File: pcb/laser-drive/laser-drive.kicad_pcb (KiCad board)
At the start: 2 copper layers, 28.6 x 32.4 mm, 28 parts, among them J1 CONN_01X03, P1 LaserOut, Q1 BCP5616Q, Q2 MTM232270, U2 MIC920

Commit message: o Change footprint trimmer to actual size.
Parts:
- RV1: footprint Potentiometers:Potentiometer_WirePads -> Potentiometers:Potentiometer_WirePads_Small
- moved RV1 5.26 mm to (95.9, 48.3)
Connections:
- net LASER_DATA renamed Net-(J1-Pad2)
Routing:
- net GND: track 127.1 -> 130.9 mm
- net /VRef: track 10.4 -> 12.8 mm

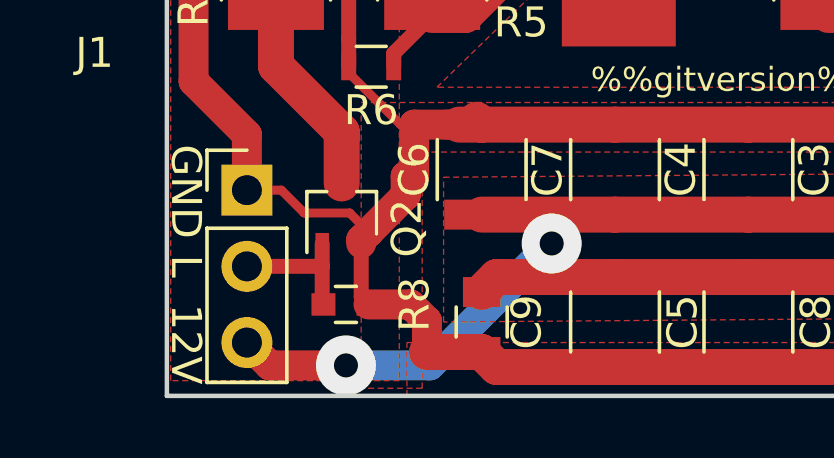
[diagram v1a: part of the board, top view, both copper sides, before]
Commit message: o Update footprint resistor.
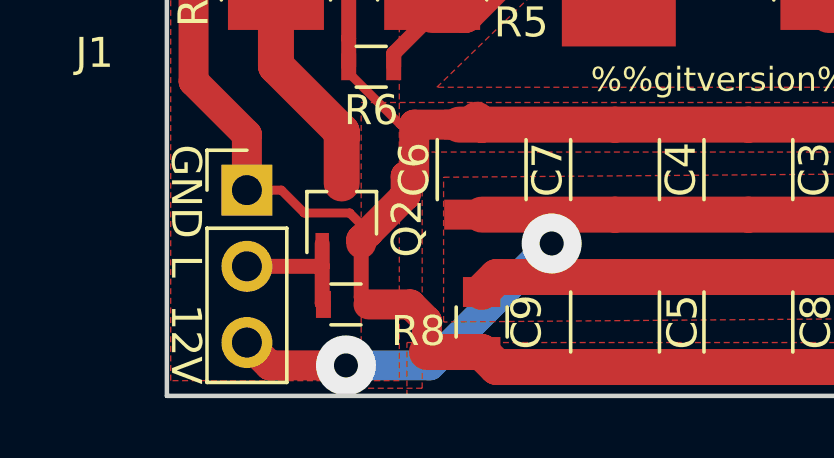
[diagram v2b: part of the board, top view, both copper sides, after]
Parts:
- R8: value 100k -> 1k; footprint Capacitors_SMD:C_0603 -> Resistors_SMD:R_0603
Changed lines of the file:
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@@
-(kicad_pcb (version 20170123) (host pcbnew "(2017-03-23 revision f2763e90e)-master")
+(kicad_pcb (version 20170123) (host pcbnew "(2017-04-01 revision 6eb2000b6)-master")
   (general
     (links 48)
@@
     )
   )
-  (module Capacitors_SMD:C_0603 (layer F.Cu)
-    (at 89.154 74.422 180)
-    (descr "Capacitor SMD 0603, reflow soldering, AVX (see smccp.pdf)")
-    (tags "capacitor 0603")
-    (attr smd)
-    (fp_text reference R8 (at -2.286 0 90) (layer F.SilkS)
-      (effects (font (size 1 1) (thickness 0.15)))
-    )
-    (fp_text value 100k (at 0 1.5 180) (layer F.Fab)
-      (effects (font (size 1 1) (thickness 0.15)))
-    )
-    (fp_line (start 1.4 0.65) (end -1.4 0.65) (layer F.CrtYd) (width 0.05))
-    (fp_line (start 1.4 0.65) (end 1.4 -0.65) (layer F.CrtYd) (width 0.05))
-    (fp_line (start -1.4 -0.65) (end -1.4 0.65) (layer F.CrtYd) (width 0.05))
-    (fp_line (start -1.4 -0.65) (end 1.4 -0.65) (layer F.CrtYd) (width 0.05))
-    (fp_line (start 0.35 0.6) (end -0.35 0.6) (layer F.SilkS) (width 0.12))
-    (fp_line (start -0.35 -0.6) (end 0.35 -0.6) (layer F.SilkS) (width 0.12))
-    (fp_line (start -0.8 -0.4) (end 0.8 -0.4) (layer F.Fab) (width 0.1))
-    (fp_line (start 0.8 -0.4) (end 0.8 0.4) (layer F.Fab) (width 0.1))
-    (fp_line (start 0.8 0.4) (end -0.8 0.4) (layer F.Fab) (width 0.1))
-    (fp_line (start -0.8 0.4) (end -0.8 -0.4) (layer F.Fab) (width 0.1))
-    (fp_text user %R (at 0 -1.5 180) (layer F.Fab)
-      (effects (font (size 1 1) (thickness 0.15)))
-    )
-    (pad 2 smd rect (at 0.75 0 180) (size 0.8 0.75) (layers F.Cu F.Paste F.Mask)
-      (net 12 "Net-(J1-Pad2)"))
-    (pad 1 smd rect (at -0.75 0 180) (size 0.8 0.75) (layers F.Cu F.Paste F.Mask)
-      (net 1 GND))
-    (model Capacitors_SMD.3dshapes/C_0603.wrl
-      (at (xyz 0 0 0))
-      (scale (xyz 1 1 1))
-      (rotate (xyz 0 0 0))
-    )
-  )
   (module TO_SOT_Packages_SMD:SOT-323_SC-70 (layer F.Cu)
     (at 89.012 71.39 90)
@@
       (scale (xyz 1 1 1))
       (rotate (xyz 0 0 0))
+    )
+  )
+  (module Resistors_SMD:R_0603 (layer F.Cu)
+    (at 89.154 74.422 180)
+    (descr "Resistor SMD 0603, reflow soldering, Vishay (see dcrcw.pdf)")
+    (tags "resistor 0603")
+    (attr smd)
+    (fp_text reference R8 (at -2.413 -0.889 180) (layer F.SilkS)
+      (effects (font (size 1 1) (thickness 0.15)))
+    )
+    (fp_text value 1k (at 0 1.5 180) (layer F.Fab)
+      (effects (font (size 1 1) (thickness 0.15)))
+    )
+    (fp_text user %R (at 0 -1.45 180) (layer F.Fab)
+      (effects (font (size 1 1) (thickness 0.15)))
+    )
+    (fp_line (start -0.8 0.4) (end -0.8 -0.4) (layer F.Fab) (width 0.1))
+    (fp_line (start 0.8 0.4) (end -0.8 0.4) (layer F.Fab) (width 0.1))
+    (fp_line (start 0.8 -0.4) (end 0.8 0.4) (layer F.Fab) (width 0.1))
+    (fp_line (start -0.8 -0.4) (end 0.8 -0.4) (layer F.Fab) (width 0.1))
+    (fp_line (start 0.5 0.68) (end -0.5 0.68) (layer F.SilkS) (width 0.12))
+    (fp_line (start -0.5 -0.68) (end 0.5 -0.68) (layer F.SilkS) (width 0.12))
+    (fp_line (start -1.25 -0.7) (end 1.25 -0.7) (layer F.CrtYd) (width 0.05))
+    (fp_line (start -1.25 -0.7) (end -1.25 0.7) (layer F.CrtYd) (width 0.05))
+    (fp_line (start 1.25 0.7) (end 1.25 -0.7) (layer F.CrtYd) (width 0.05))
+    (fp_line (start 1.25 0.7) (end -1.25 0.7) (layer F.CrtYd) (width 0.05))
+    (pad 1 smd rect (at -0.75 0 180) (size 0.5 0.9) (layers F.Cu F.Paste F.Mask)
+      (net 1 GND))
+    (pad 2 smd rect (at 0.75 0 180) (size 0.5 0.9) (layers F.Cu F.Paste F.Mask)
+      (net 12 "Net-(J1-Pad2)"))
+    (model Resistors_SMD.3dshapes/R_0603.wrl
+      (at (xyz 0 0 0))
+      (scale (xyz 1 1 1))
+      (rotate (xyz 0 0 0))
